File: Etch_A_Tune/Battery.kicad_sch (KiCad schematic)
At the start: 16 parts, among them IC1 BQ25170DSGR, U1 BQ297xy, U2 CSD16406Q3, U3 CSD16406Q3

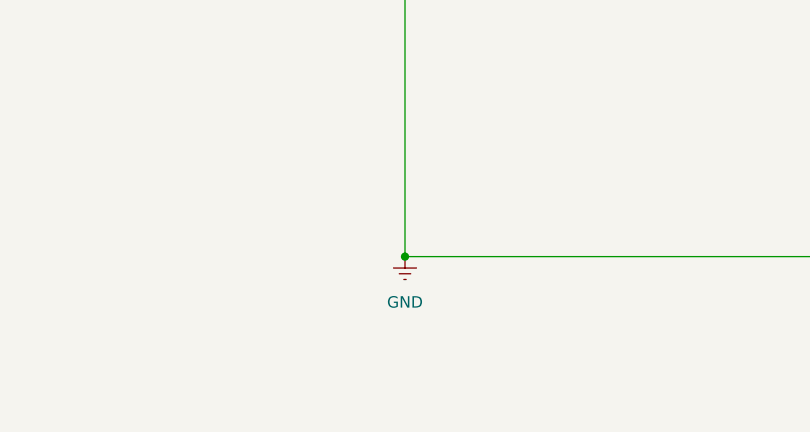
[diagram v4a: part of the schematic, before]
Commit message: V.04 Schematic
added 64 pin header LEDS
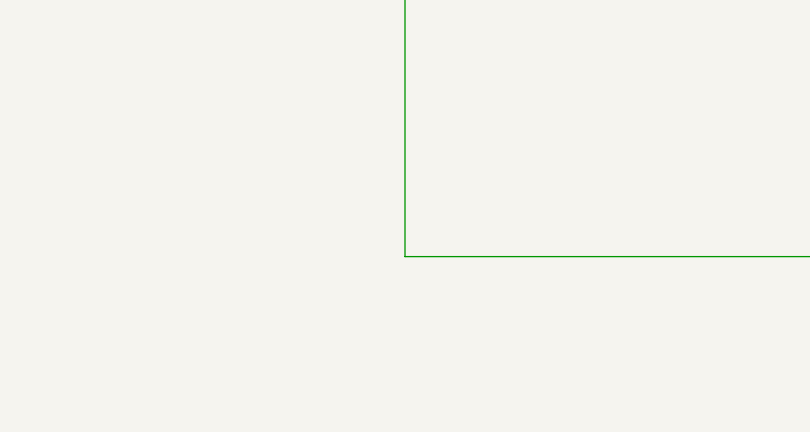
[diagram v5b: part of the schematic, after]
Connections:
- net GND: no longer BT1.N, C3.2, U1.4 (VSS), U2.1, U2.2, U2.3
- new net: BT1.N, C3.2, U1.4 (VSS), U2.1, U2.2, U2.3
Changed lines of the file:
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@@
-	)
-	(junction
-		(at 245.11 215.9)
-		(diameter 0)
-		(color 0 0 0 0)
 	)
 	(junction
@@
 					(unit 1)
 				)
-			)
-		)
-	)
-	(symbol
-		(lib_id "power:Earth")
-		(at 245.11 215.9 0)
-		(unit 1)
-		(exclude_from_sim no)
-		(in_bom yes)
-		(on_board yes)
-		(dnp no)
-		(fields_autoplaced yes)
-		(property "Reference" "#PWR06"
-			(at 245.11 222.25 0)
-			(effects
-				(font
-					(size 1.27 1.27)
-				)
-				(hide yes)
-			)
-		)
-		(property "Value" "GND"
-			(at 245.11 220.98 0)
-			(effects
-				(font
-					(size 1.27 1.27)
-				)
-			)
-		)
-		(property "Footprint" ""
-			(at 245.11 215.9 0)
-			(effects
-				(font
-					(size 1.27 1.27)
-				)
-				(hide yes)
-			)
-		)
-		(property "Datasheet" "~"
-			(at 245.11 215.9 0)
-			(effects
-				(font
-					(size 1.27 1.27)
-				)
-				(hide yes)
-			)
-		)
-		(property "Description" "Power symbol creates a global label with name \"Earth\""
-			(at 245.11 215.9 0)
-			(effects
-				(font
-					(size 1.27 1.27)
-				)
-				(hide yes)
-			)
-		)
-		(pin "1"
-		)
-		(instances
-			(project "Etch_A_Tune"
-				(path "/b4cdadf2-c4fe-48fe-ba6a-e15d1cad03b2/dd28cf9e-f503-4fc4-9cf8-d81b8295f9d5"
-					(reference "#PWR06")
-					(unit 1)
-				)

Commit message: Updated schematic
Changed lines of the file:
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@@
 	(text "800-MA LINEAR BATTERY CHARGER \n"
 		(exclude_from_sim no)
-		(at 36.83 19.05 0)
+		(at 62.23 90.678 0)
 		(effects
 			(font

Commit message: Final Layout before routing
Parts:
- added R26, R28: 0, Resistor_SMD:R_0603_1608Metric, symbol Device:R
- C1, C2: value C -> 1uF; footprint (none) -> Capacitor_SMD:C_0603_1608Metric
- C3: value C -> .1uF; footprint (none) -> Capacitor_SMD:C_0603_1608Metric
- R1: value R -> 24k; footprint (none) -> Resistor_SMD:R_0603_1608Metric
- R2: value R -> 604; footprint (none) -> Resistor_SMD:R_0603_1608Metric
- R3: value R -> 330; footprint (none) -> Resistor_SMD:R_0603_1608Metric
- R4: value R -> 2.2k; footprint (none) -> Resistor_SMD:R_0603_1608Metric
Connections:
- net BAT_V_SENSE: now also R26.1; no longer BT1.P, C2.1, IC1.8 (OUT), R3.1, TP3.1
- net USB_Power: now also R28.1; no longer C1.1, IC1.1 (IN)
- new net: C1.1, IC1.1 (IN), R28.2
- new net PACK+: BT1.P, C2.1, IC1.8 (OUT), R26.2, R3.1, TP3.1
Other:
- moved on the sheet: BT1, C1

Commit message: Update
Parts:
- removed IC1: BQ25170DSGR, BQ25170DSGR:SON50P200X200X80-9N, symbol SamacSys_Parts:BQ25170DSGR
- added R31: 10k, Resistor_SMD:R_0603_1608Metric, symbol Device:R
- added R32, R33, R34, R35, R36, R37, R38: 0, Resistor_SMD:R_0603_1608Metric, symbol Device:R
- added U6: BQ25170DSGR, BQ25170DSGR:SON50P200X200X80-9N, symbol BQ25170DSGR:BQ25170DSGR
- BT1: Availability In Stock -> (none); Check_prices https://www.snapeda.com/parts/1042P/Keystone/view-part/?ref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 -> (none); Description_1 SMT Polarized Battery Holder for 18650 Battery | Keystone E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 -> (none); MF Keystone Electronics -> (none); MP 1042P -> (none); Package None -> (none); Price None -> (none); SnapEDA_Link https://www.snapeda.com/parts/1042P/Keystone/view-part/?ref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 -> (none)
- R1: value 24k -> 27k
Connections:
- net BAT_DIAG: now also R35.2
- net CHARGE_GATE: now also R33.2; no longer U3.4
- net DISCHARGE_GATE: now also R34.1; no longer U2.4
- net GND: now also R31.2, R32.2, R37.1, R38.1, U6.4 (GND), U6.9 (EXP)
- net PACK+: now also U6.8 (OUT)
- net PG: now also R36.2
- net at BT1.N, C3.2, U1.4 (VSS)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: now also R32.1
- net at C1.1, R28.2: now also U6.1 (IN)
- net at R2.1: now also U6.2 (ISET)
- net at R1.1: now also U6.7 (VSET)
- net USB_Power renamed USB_Charge
- new net: R33.1, U3.4
- new net: R31.1, U6.3 (TS)
- new net: R36.1, R37.2, U6.6 (~{PG})
- new net: R34.2, U2.4
- new net: R35.1, R38.2, U6.5 (STAT)
